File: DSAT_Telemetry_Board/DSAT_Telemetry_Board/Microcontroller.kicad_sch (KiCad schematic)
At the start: 20 parts, among them J4 USB_B_Micro, J5 Conn_01x04_Male, SW1 SW_Push, SW2 SW_SPDT, U5 STM32L433RCTx, Y1 16MHz

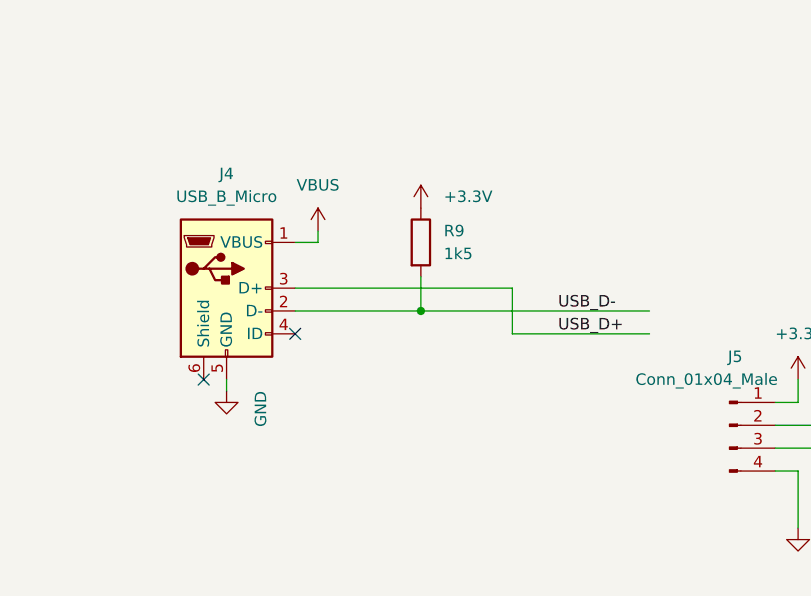
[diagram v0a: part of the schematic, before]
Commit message: Added Watchdog Timer Footprint
Added custom footprint for watchdog timer
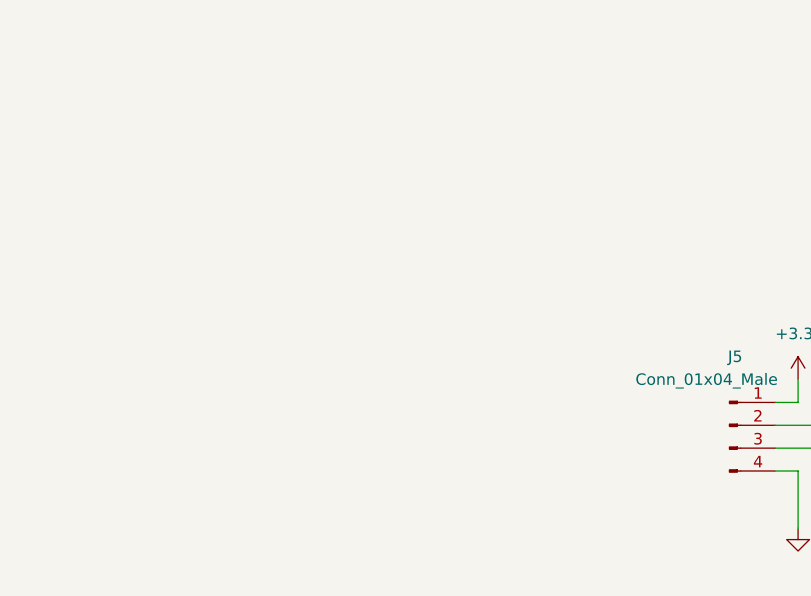
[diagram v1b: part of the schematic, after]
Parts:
- removed J4: USB_B_Micro, symbol Connector:USB_B_Micro
- removed R9: 1k5, Resistor_SMD:R_0402_1005Metric_Pad0.72x0.64mm_HandSolder, symbol Device:R
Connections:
- no-connect marks 2 -> 0
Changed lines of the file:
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@@
   (junction (at 190.5 36.83) (diameter 0) (color 0 0 0 0)
   )
-  (junction (at 87.63 81.28) (diameter 0) (color 0 0 0 0)
-  )
   (junction (at 218.44 27.94) (diameter 0) (color 0 0 0 0)
   )
@@
   (junction (at 223.52 83.82) (diameter 0) (color 0 0 0 0)
   )
-  (no_connect (at 73.66 83.82))
-  (no_connect (at 63.5 88.9))
   (wire (pts (xy 182.88 27.94) (xy 182.88 26.67))
     (stroke (width 0) (type default) (color 0 0 0 0))
@@
     (stroke (width 0) (type default) (color 0 0 0 0))
   )
-  (wire (pts (xy 87.63 81.28) (xy 113.03 81.28))
-    (stroke (width 0) (type default) (color 0 0 0 0))
-  )
   (wire (pts (xy 240.03 104.14) (xy 243.84 104.14))
     (stroke (width 0) (type default) (color 0 0 0 0))
@@
     (stroke (width 0) (type default) (color 0 0 0 0))
   )
-  (wire (pts (xy 76.2 72.39) (xy 76.2 73.66))
-    (stroke (width 0) (type default) (color 0 0 0 0))
-  )
   (wire (pts (xy 180.34 134.62) (xy 180.34 140.97))
     (stroke (width 0) (type default) (color 0 0 0 0))
@@
     (stroke (width 0) (type default) (color 0 0 0 0))
   )
-  (wire (pts (xy 73.66 81.28) (xy 87.63 81.28))
-    (stroke (width 0) (type default) (color 0 0 0 0))
-  )
   (wire (pts (xy 210.82 48.26) (xy 210.82 49.53))
     (stroke (width 0) (type default) (color 0 0 0 0))
@@
     (stroke (width 0) (type default) (color 0 0 0 0))
   )
-  (wire (pts (xy 76.2 73.66) (xy 73.66 73.66))
-    (stroke (width 0) (type default) (color 0 0 0 0))
-  )
   (wire (pts (xy 218.44 38.1) (xy 204.47 38.1))
     (stroke (width 0) (type default) (color 0 0 0 0))
@@
     (stroke (width 0) (type default) (color 0 0 0 0))
   )
-  (wire (pts (xy 97.79 78.74) (xy 97.79 83.82))
-    (stroke (width 0) (type default) (color 0 0 0 0))
-  )
   (wire (pts (xy 147.32 73.66) (xy 160.02 73.66))
     (stroke (width 0) (type default) (color 0 0 0 0))
@@
     (stroke (width 0) (type default) (color 0 0 0 0))
   )
-  (wire (pts (xy 87.63 77.47) (xy 87.63 81.28))
-    (stroke (width 0) (type default) (color 0 0 0 0))
-  )
   (wire (pts (xy 245.11 27.94) (xy 245.11 29.21))
     (stroke (width 0) (type default) (color 0 0 0 0))
@@
     (stroke (width 0) (type default) (color 0 0 0 0))
   )
-  (wire (pts (xy 97.79 83.82) (xy 113.03 83.82))
-    (stroke (width 0) (type default) (color 0 0 0 0))
-  )
   (wire (pts (xy 177.8 140.97) (xy 175.26 140.97))
     (stroke (width 0) (type default) (color 0 0 0 0))
@@
     (stroke (width 0) (type default) (color 0 0 0 0))
   )
-  (wire (pts (xy 66.04 88.9) (xy 66.04 90.17))
-    (stroke (width 0) (type default) (color 0 0 0 0))
-  )
   (wire (pts (xy 133.35 36.83) (xy 133.35 39.37))
     (stroke (width 0) (type default) (color 0 0 0 0))
@@
   )
   (wire (pts (xy 134.62 83.82) (xy 134.62 96.52))
-    (stroke (width 0) (type default) (color 0 0 0 0))
-  )
-  (wire (pts (xy 73.66 78.74) (xy 97.79 78.74))
     (stroke (width 0) (type default) (color 0 0 0 0))
   )
@@
     (effects (font (size 1.27 1.27)) (justify left bottom))
   )
-  (label "USB_D-" (at 102.87 81.28 0)
-    (effects (font (size 1.27 1.27)) (justify left bottom))
-  )
   (label "Clock_Out" (at 195.58 78.74 0)
     (effects (font (size 1.27 1.27)) (justify left bottom))
   )
-  (label "USB_D+" (at 102.87 83.82 0)
-    (effects (font (size 1.27 1.27)) (justify left bottom))
-  )
   (label "DEBUG_DIO" (at 135.89 81.28 0)
     (effects (font (size 1.27 1.27)) (justify left bottom))
@@
     (pin "1")
   )
-  (symbol (lib_id "Connector:USB_B_Micro") (at 66.04 78.74 0) (unit 1)
-    (in_bom yes) (on_board yes) (fields_autoplaced)
-    (property "Reference" "J4" (id 0) (at 66.04 66.04 0))
-    (property "Value" "USB_B_Micro" (id 1) (at 66.04 68.58 0))
-    (property "Footprint" "" (id 2) (at 69.85 80.01 0)
-      (effects (font (size 1.27 1.27)) hide)
-    )
-    (property "Datasheet" "~" (id 3) (at 69.85 80.01 0)
-      (effects (font (size 1.27 1.27)) hide)
-    )
-    (pin "1")
-    (pin "2")
-    (pin "3")
-    (pin "4")
-    (pin "5")
-    (pin "6")
-  )
   (symbol (lib_id "power:GND") (at 245.11 39.37 0) (unit 1)
     (in_bom yes) (on_board yes) (fields_autoplaced)
@@
     )
     (property "Datasheet" "https://www.digikey.com/en/products/detail/murata-electronics/GRM033R60J105MEA2D/4213369" (id 3) (at 153.67 33.02 0)
-      (effects (font (size 1.27 1.27)) hide)
-    )
-    (pin "1")
-    (pin "2")
-  )
-  (symbol (lib_id "power:GND") (at 66.04 90.17 0) (unit 1)
-    (in_bom yes) (on_board yes)
-    (property "Reference" "#PWR0123" (id 0) (at 66.04 96.52 0)
-      (effects (font (size 1.27 1.27)) hide)
-    )
-    (property "Value" "GND" (id 1) (at 69.85 90.17 90)
-      (effects (font (size 1.27 1.27)) (justify right))
-    )
-    (property "Footprint" "" (id 2) (at 66.04 90.17 0)
-      (effects (font (size 1.27 1.27)) hide)
-    )
-    (property "Datasheet" "" (id 3) (at 66.04 90.17 0)
-      (effects (font (size 1.27 1.27)) hide)
-    )
-    (pin "1")
-  )
-  (symbol (lib_id "Device:R") (at 87.63 73.66 0) (unit 1)
-    (in_bom yes) (on_board yes) (fields_autoplaced)
-    (property "Reference" "R9" (id 0) (at 90.17 72.3899 0)
-      (effects (font (size 1.27 1.27)) (justify left))
-    )
-    (property "Value" "1k5" (id 1) (at 90.17 74.9299 0)
-      (effects (font (size 1.27 1.27)) (justify left))
-    )
-    (property "Footprint" "Resistor_SMD:R_0402_1005Metric_Pad0.72x0.64mm_HandSolder" (id 2) (at 85.852 73.66 90)
-      (effects (font (size 1.27 1.27)) hide)
-    )
-    (property "Datasheet" "https://www.digikey.com/en/products/detail/panasonic-electronic-components/ERA-8ARW102V/5141111" (id 3) (at 87.63 73.66 0)
       (effects (font (size 1.27 1.27)) hide)
     )
@@
     (pin "1")
     (pin "2")
-  )
-  (symbol (lib_id "power:VBUS") (at 76.2 72.39 0) (unit 1)
-    (in_bom yes) (on_board yes) (fields_autoplaced)
-    (property "Reference" "#PWR0122" (id 0) (at 76.2 76.2 0)
-      (effects (font (size 1.27 1.27)) hide)
-    )
-    (property "Value" "VBUS" (id 1) (at 76.2 67.31 0))
-    (property "Footprint" "" (id 2) (at 76.2 72.39 0)
-      (effects (font (size 1.27 1.27)) hide)
-    )
-    (property "Datasheet" "" (id 3) (at 76.2 72.39 0)
-      (effects (font (size 1.27 1.27)) hide)
-    )
-    (pin "1")
   )
   (symbol (lib_id "Switch:SW_Push") (at 210.82 54.61 270) (unit 1)
@@
       (effects (font (size 1.27 1.27)) hide)
     )
-    (pin "1")
-  )
-  (symbol (lib_id "power:+3.3V") (at 87.63 69.85 0) (mirror y) (unit 1)
-    (in_bom yes) (on_board yes) (fields_autoplaced)
-    (property "Reference" "#PWR0124" (id 0) (at 87.63 73.66 0)
-      (effects (font (size 1.27 1.27)) hide)
-    )
-    (property "Value" "+3.3V" (id 1) (at 90.17 68.5799 0)
-      (effects (font (size 1.27 1.27)) (justify right))
-    )
-    (property "Footprint" "" (id 2) (at 87.63 69.85 0)
-      (effects (font (size 1.27 1.27)) hide)
-    )
-    (property "Datasheet" "" (id 3) (at 87.63 69.85 0)
-      (effects (font (size 1.27 1.27)) hide)
-    )

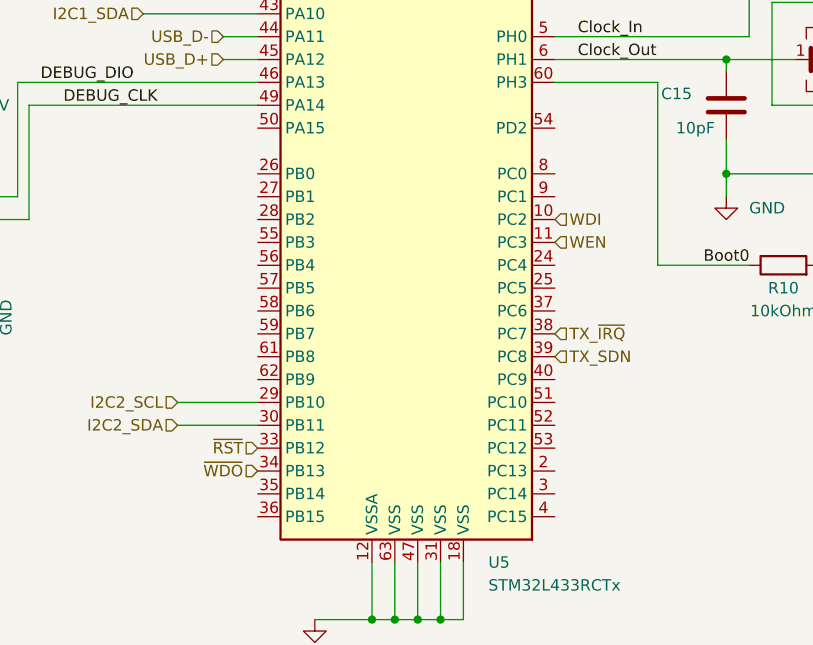
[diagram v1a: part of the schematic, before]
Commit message: Fixed PCB
Added new voltage regulator, reorganized everything, added new lines, fixed most DRC issues. Added ground and power pours. Added more vias.
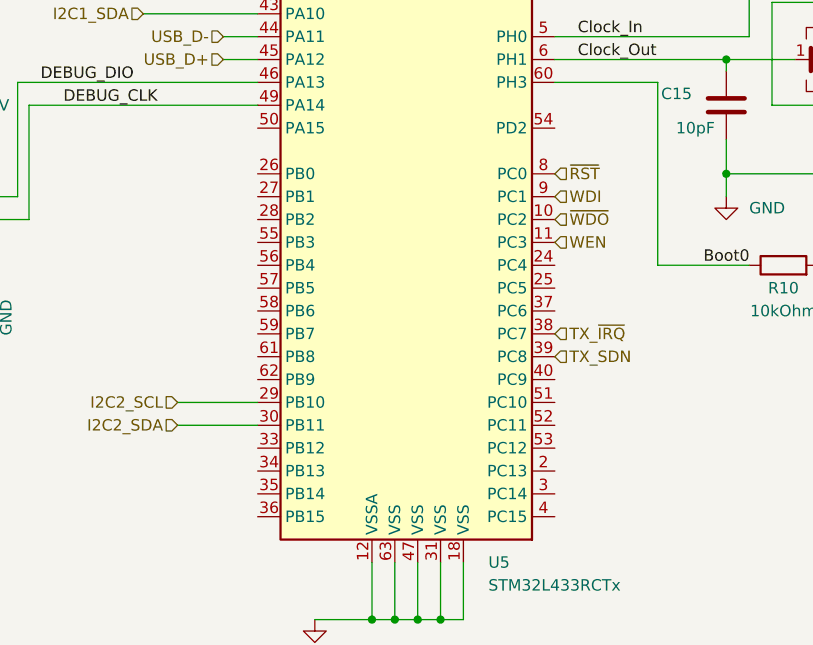
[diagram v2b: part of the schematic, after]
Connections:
- net WDI: now also U5.9 (PC1); no longer U5.10 (PC2)
- net ~{RST}: now also U5.8 (PC0); no longer U5.33 (PB12)
- net ~{WDO}: now also U5.10 (PC2); no longer U5.34 (PB13)
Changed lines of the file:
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@@
     (effects (font (size 1.27 1.27)) (justify left bottom))
   )
-  (hierarchical_label "~{WDO}" (shape input) (at 160.02 124.46 180)
-    (effects (font (size 1.27 1.27)) (justify right))
+  (hierarchical_label "~{WDO}" (shape input) (at 193.04 96.52 0)
+    (effects (font (size 1.27 1.27)) (justify left))
   )
   (hierarchical_label "USB_D+" (shape input) (at 156.21 78.74 180)
@@
   (hierarchical_label "TX_SDN" (shape input) (at 193.04 111.76 0)
     (effects (font (size 1.27 1.27)) (justify left))
-  )
-  (hierarchical_label "~{RST}" (shape input) (at 160.02 121.92 180)
-    (effects (font (size 1.27 1.27)) (justify right))
   )
   (hierarchical_label "WEN" (shape input) (at 193.04 99.06 0)
@@
     (effects (font (size 1.27 1.27)) (justify right))
   )
+  (hierarchical_label "~{RST}" (shape input) (at 193.04 91.44 0)
+    (effects (font (size 1.27 1.27)) (justify left))
+  )
   (hierarchical_label "USB_D-" (shape input) (at 156.21 76.2 180)
     (effects (font (size 1.27 1.27)) (justify right))
@@
   (hierarchical_label "I2C1_SDA" (shape input) (at 147.32 73.66 180)
     (effects (font (size 1.27 1.27)) (justify right))
+  )
+  (hierarchical_label "WDI" (shape input) (at 193.04 93.98 0)
+    (effects (font (size 1.27 1.27)) (justify left))
   )
   (hierarchical_label "TX_SDO" (shape input) (at 160.02 63.5 180)
@@
     (effects (font (size 1.27 1.27)) (justify right))
   )
-  (hierarchical_label "WDI" (shape input) (at 193.04 96.52 0)
-    (effects (font (size 1.27 1.27)) (justify left))
-  )
   (symbol (lib_id "power:+3.3V") (at 242.57 99.06 270) (mirror x) (unit 1)
